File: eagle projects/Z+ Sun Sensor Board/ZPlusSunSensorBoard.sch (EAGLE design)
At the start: 53 parts, among them Q1 BSS138PS,115, Q2 BSS138PS,115, Q7 BSS138PS,115, Q8 BSS138PS,115, U1 ADS7841E_2K5, U2 REF194GSZ-REEL7, U3 TLV9054IDR, U4 LM20BIM7X_NOPB

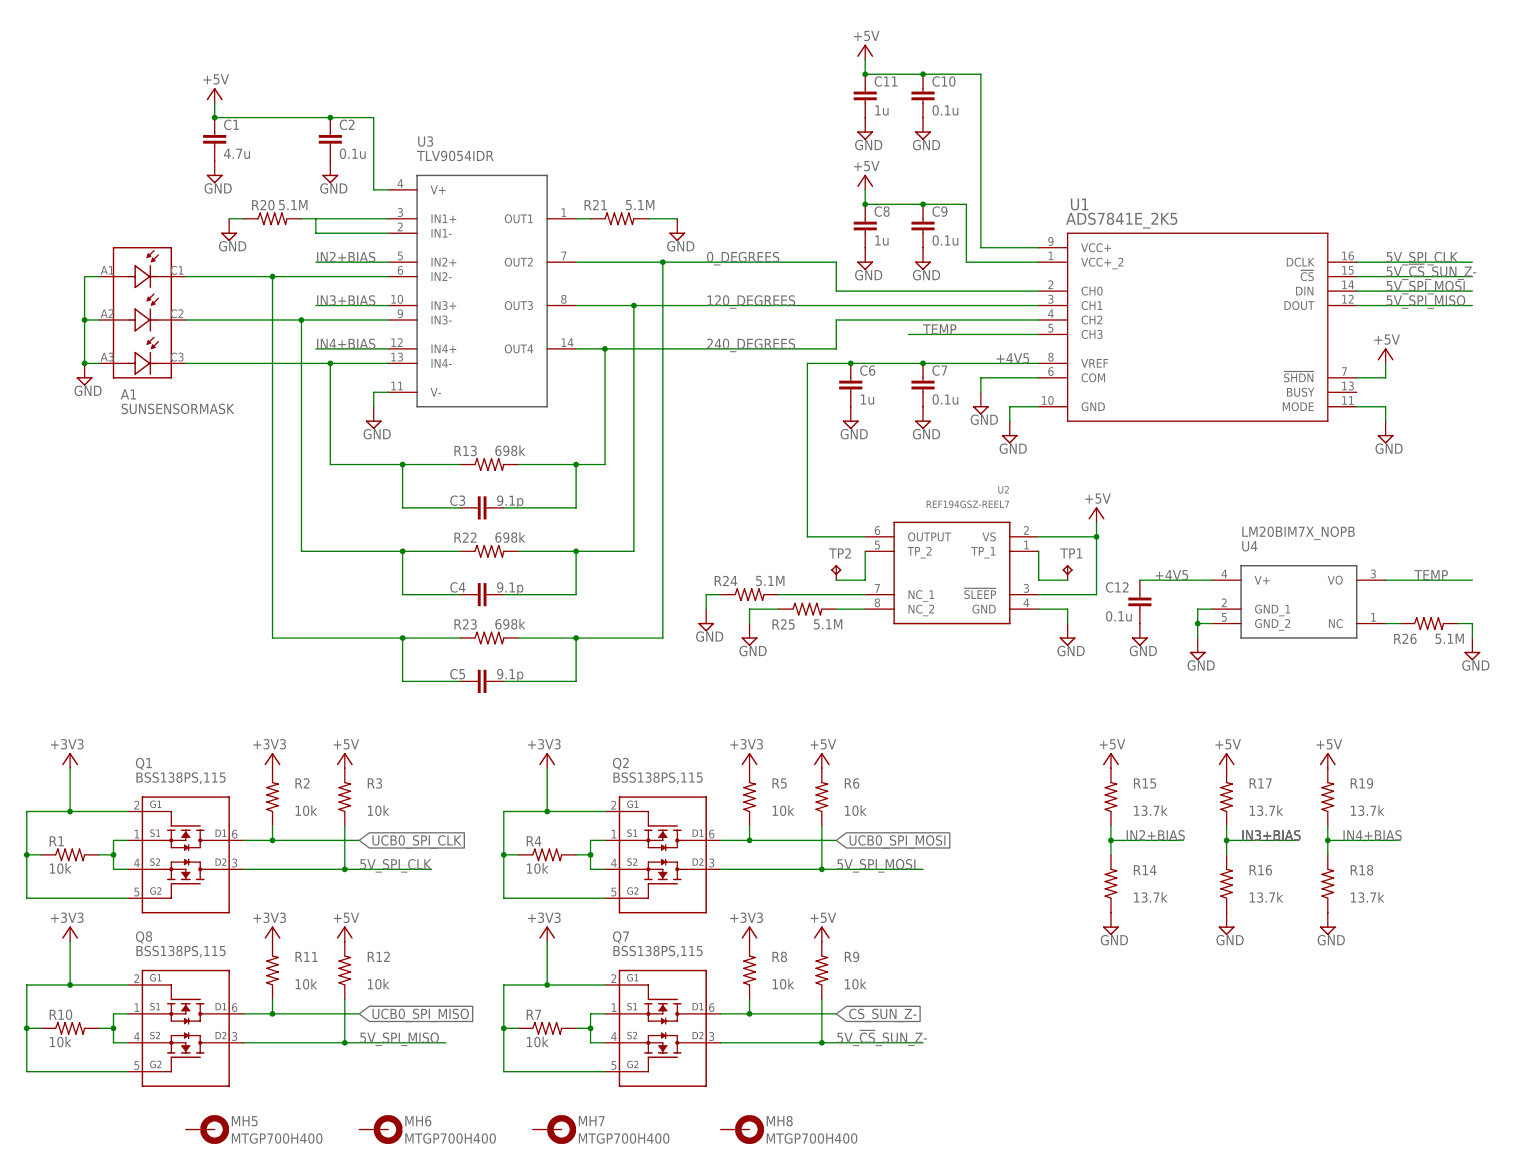
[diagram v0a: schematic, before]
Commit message: Added connector pins
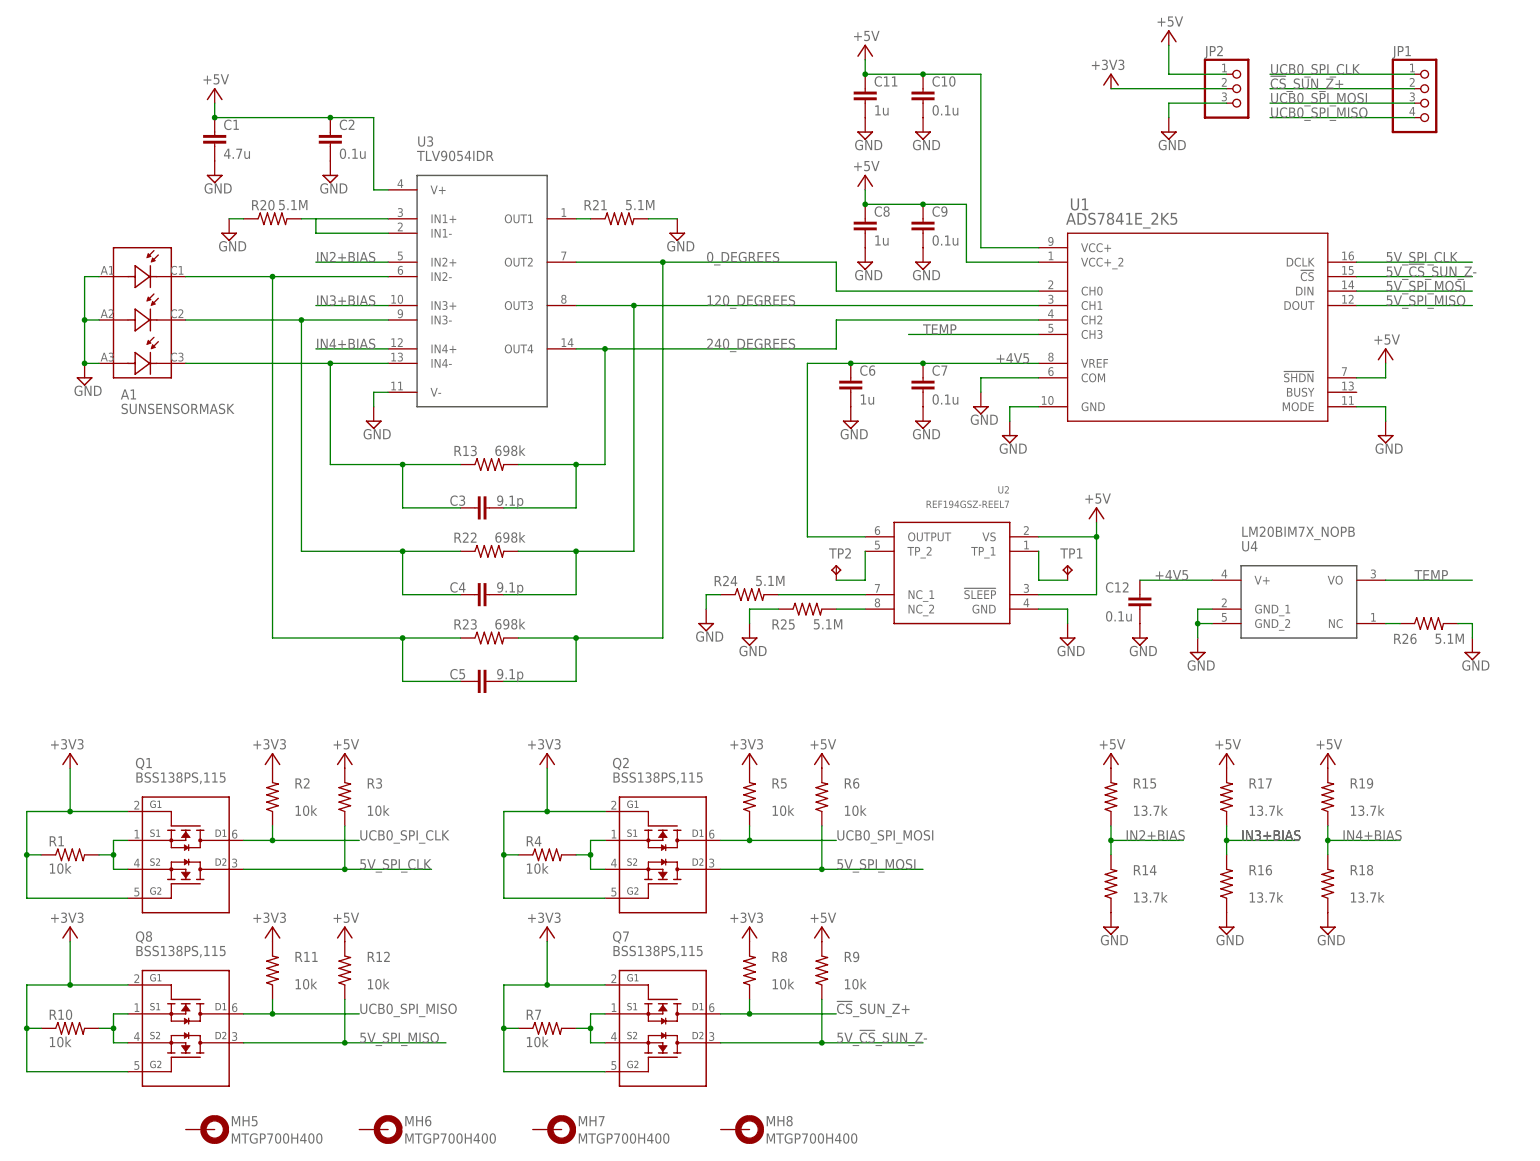
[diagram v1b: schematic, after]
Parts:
- added JP1: (no value), pinhead:PINHD-1X4
- added JP2: (no value), pinhead:PINHD-1X3
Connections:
- removed net !CS!_SUN_Z-: Q7.D1, R8.1
- new net !CS!_SUN_Z+: JP1.2, Q7.D1, R8.1
- net +3V3: now also JP2.2
- net +5V: now also JP2.1
- net GND: now also JP2.3
- net UCB0_SPI_CLK: now also JP1.1
- net UCB0_SPI_MISO: now also JP1.4
- net UCB0_SPI_MOSI: now also JP1.3
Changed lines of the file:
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@@
 <part name="C12" library="rcl" library_urn="urn:adsk.eagle:library:334" deviceset="C-EU" device="C0603" package3d_urn="urn:adsk.eagle:package:23616/2" value="0.1u"/>
 <part name="SUPPLY24" library="supply2" library_urn="urn:adsk.eagle:library:372" deviceset="GND" device=""/>
+<part name="JP1" library="pinhead" library_urn="urn:adsk.eagle:library:325" deviceset="PINHD-1X4" device="" package3d_urn="urn:adsk.eagle:package:22407/2"/>
+<part name="JP2" library="pinhead" library_urn="urn:adsk.eagle:library:325" deviceset="PINHD-1X3" device="" package3d_urn="urn:adsk.eagle:package:22458/2"/>
+<part name="P+4" library="supply1" library_urn="urn:adsk.eagle:library:371" deviceset="+5V" device=""/>
+<part name="+3V9" library="supply1" library_urn="urn:adsk.eagle:library:371" deviceset="+3V3" device=""/>
+<part name="SUPPLY25" library="supply2" library_urn="urn:adsk.eagle:library:372" deviceset="GND" device=""/>
 </parts>
 <sheets>
@@
 <attribute name="VALUE" x="203.835" y="93.345" size="1.778" layer="96"/>
 </instance>
+<instance part="JP1" gate="A" x="256.54" y="190.5" smashed="yes">
+<attribute name="NAME" x="250.19" y="198.755" size="1.778" layer="95"/>
+<attribute name="VALUE" x="250.19" y="182.88" size="1.778" layer="96"/>
+</instance>
+<instance part="JP2" gate="A" x="223.52" y="193.04" smashed="yes">
+<attribute name="NAME" x="217.17" y="198.755" size="1.778" layer="95"/>
+<attribute name="VALUE" x="217.17" y="185.42" size="1.778" layer="96"/>
+</instance>
+<instance part="P+4" gate="1" x="210.82" y="203.2" smashed="yes">
+<attribute name="VALUE" x="213.36" y="205.74" size="1.778" layer="96" rot="R180"/>
+</instance>
+<instance part="+3V9" gate="G$1" x="200.66" y="195.58" smashed="yes">
+<attribute name="VALUE" x="203.2" y="198.12" size="1.778" layer="96" rot="R180"/>
+</instance>
+<instance part="SUPPLY25" gate="GND" x="210.82" y="185.42" smashed="yes">
+<attribute name="VALUE" x="208.915" y="182.245" size="1.778" layer="96"/>
+</instance>
 </instances>
 <busses>
@@
 <wire x1="248.92" y1="142.24" x2="248.92" y2="144.78" width="0.1524" layer="91"/>
 </segment>
+<segment>
+<pinref part="JP2" gate="A" pin="1"/>
+<wire x1="220.98" y1="195.58" x2="210.82" y2="195.58" width="0.1524" layer="91"/>
+<wire x1="210.82" y1="195.58" x2="210.82" y2="200.66" width="0.1524" layer="91"/>
+<pinref part="P+4" gate="1" pin="+5V"/>
+</segment>
 </net>
 <net name="UCB0_SPI_MOSI" class="0">
@@
 <wire x1="137.16" y1="60.96" x2="152.4" y2="60.96" width="0.1524" layer="91"/>
 <junction x="137.16" y="60.96"/>
-<label x="152.4" y="60.96" size="1.778" layer="95" xref="yes"/>
+<label x="152.4" y="60.96" size="1.778" layer="95"/>
+</segment>
+<segment>
+<pinref part="JP1" gate="A" pin="3"/>
+<wire x1="254" y1="190.5" x2="228.6" y2="190.5" width="0.1524" layer="91"/>
+<label x="228.6" y="190.5" size="1.778" layer="95"/>
 </segment>
 </net>
@@
 <wire x1="53.34" y1="60.96" x2="68.58" y2="60.96" width="0.1524" layer="91"/>
 <junction x="53.34" y="60.96"/>
-<label x="68.58" y="60.96" size="1.778" layer="95" xref="yes"/>
+<label x="68.58" y="60.96" size="1.778" layer="95"/>
+</segment>
+<segment>
+<pinref part="JP1" gate="A" pin="1"/>
+<wire x1="254" y1="195.58" x2="228.6" y2="195.58" width="0.1524" layer="91"/>
+<label x="228.6" y="195.58" size="1.778" layer="95"/>
 </segment>
 </net>
@@
 <wire x1="53.34" y1="30.48" x2="68.58" y2="30.48" width="0.1524" layer="91"/>
 <junction x="53.34" y="30.48"/>
-<label x="68.58" y="30.48" size="1.778" layer="95" xref="yes"/>
-</segment>
-</net>
-<net name="!CS!_SUN_Z-" class="0">
+<label x="68.58" y="30.48" size="1.778" layer="95"/>
+</segment>
+<segment>
+<pinref part="JP1" gate="A" pin="4"/>
+<wire x1="254" y1="187.96" x2="228.6" y2="187.96" width="0.1524" layer="91"/>
+<label x="228.6" y="187.96" size="1.778" layer="95"/>
+</segment>
+</net>
+<net name="!CS!_SUN_Z+" class="0">
 <segment>
 <pinref part="Q7" gate="G$1" pin="D1"/>
@@
 <wire x1="137.16" y1="30.48" x2="152.4" y2="30.48" width="0.1524" layer="91"/>
 <junction x="137.16" y="30.48"/>
-<label x="152.4" y="30.48" size="1.778" layer="95" xref="yes"/>
+<label x="152.4" y="30.48" size="1.778" layer="95"/>
+</segment>
+<segment>
+<pinref part="JP1" gate="A" pin="2"/>
+<wire x1="254" y1="193.04" x2="228.6" y2="193.04" width="0.1524" layer="91"/>
+<label x="228.6" y="193.04" size="1.778" layer="95"/>
 </segment>
 </net>
@@
 <wire x1="10.16" y1="35.56" x2="17.78" y2="35.56" width="0.1524" layer="91"/>
 </segment>
+<segment>
+<pinref part="JP2" gate="A" pin="2"/>
+<wire x1="220.98" y1="193.04" x2="200.66" y2="193.04" width="0.1524" layer="91"/>
+<pinref part="+3V9" gate="G$1" pin="+3V3"/>
+</segment>
 </net>
 <net name="N$2" class="0">
@@
 <pinref part="SUPPLY24" gate="GND" pin="GND"/>
 </segment>
-</net>
+<segment>
+<pinref part="JP2" gate="A" pin="3"/>
+<wire x1="220.98" y1="190.5" x2="210.82" y2="190.5" width="0.1524" layer="91"/>
+<wire x1="210.82" y1="190.5" x2="210.82" y2="187.96" width="0.1524" layer="91"/>
+<pinref part="SUPPLY25" gate="GND" pin="GND"/>
+</segment>
+</net>

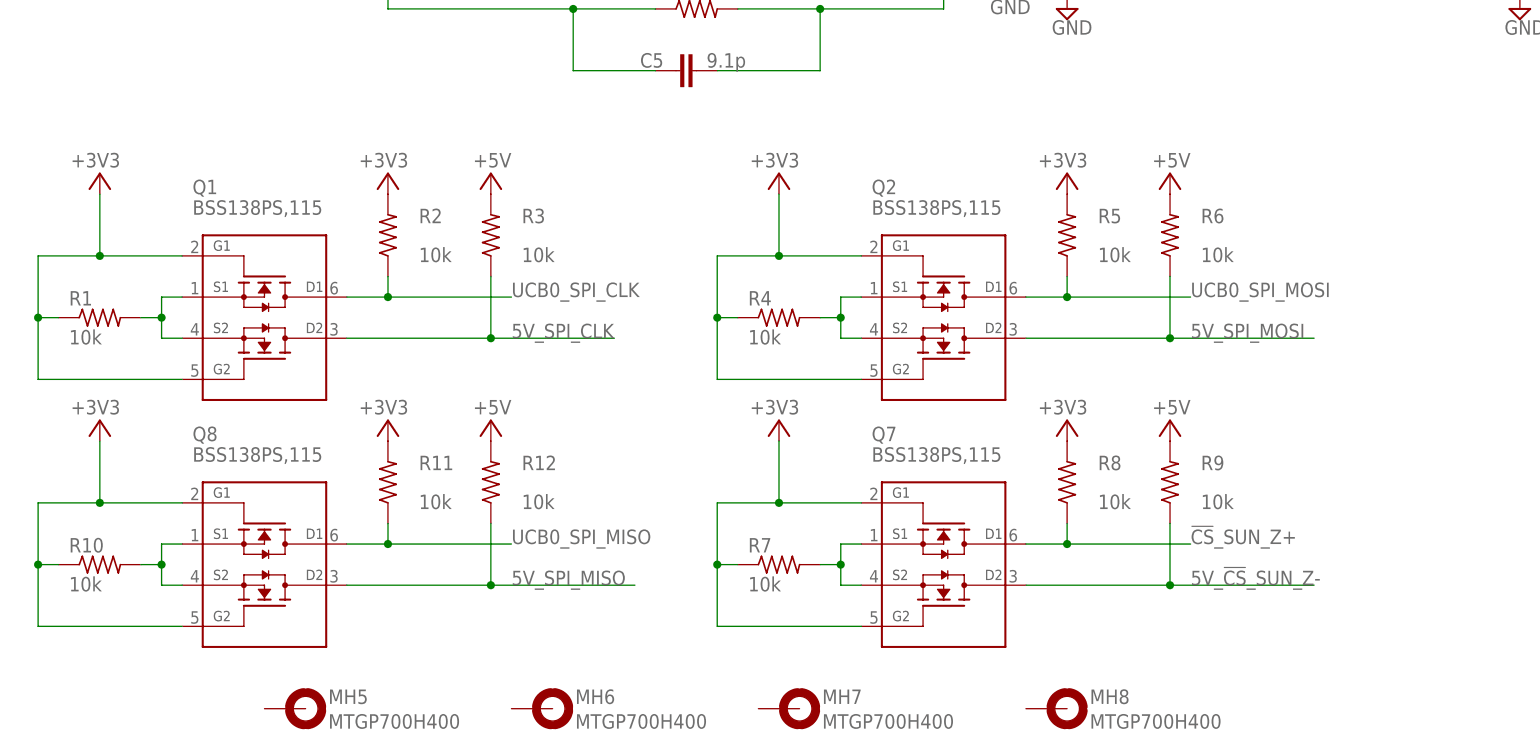
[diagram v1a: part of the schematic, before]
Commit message: Updated logic level shifter mosfet packages and board dimensions
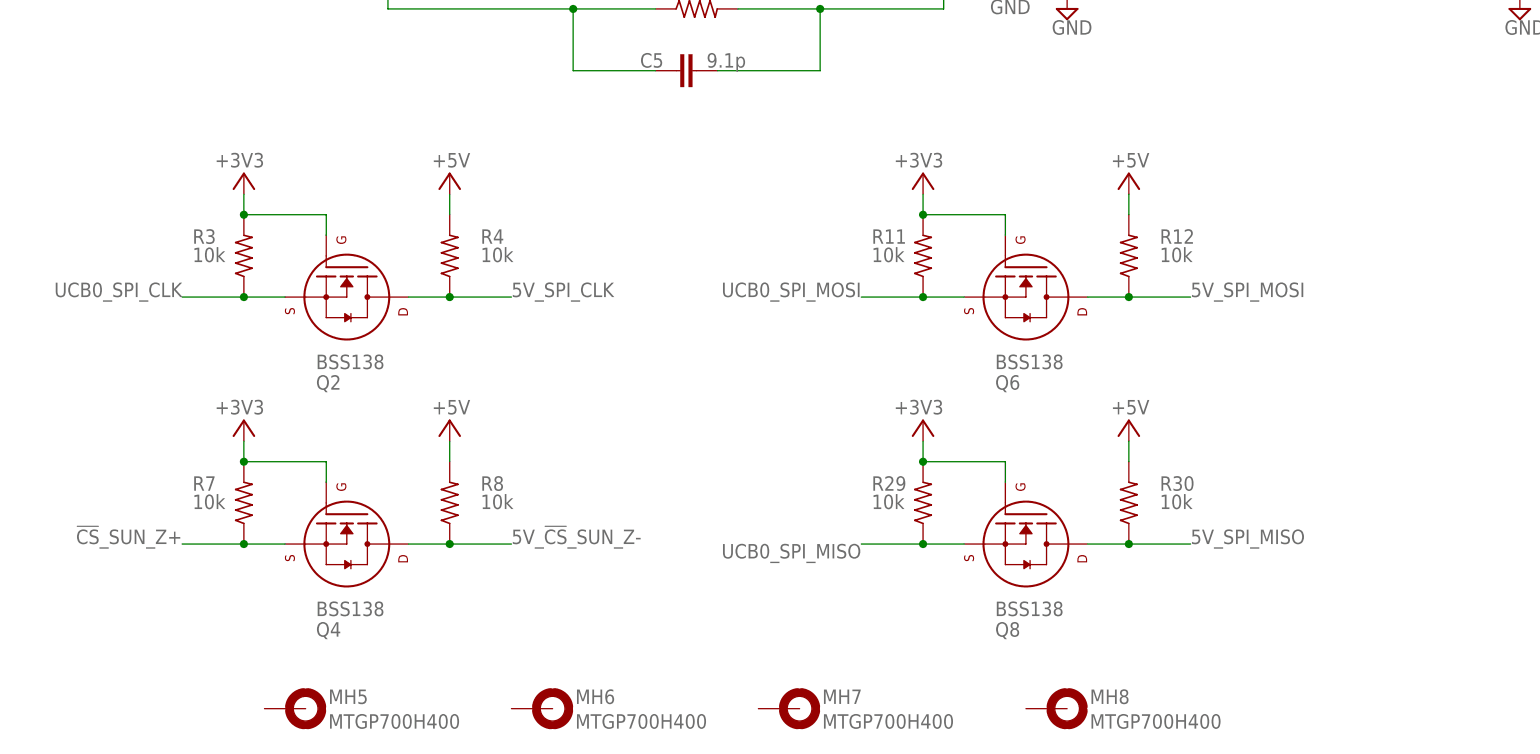
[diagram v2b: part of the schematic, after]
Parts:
- removed Q1, Q7: BSS138PS,115, my_library:BSS138PS,115
- removed R1, R10, R2, R5, R6, R9: 10k, rcl:R-US_R0402
- added Q4, Q6: BSS138, my_library:BSS138
- added R29, R30: 10k, rcl:R-US_R0603
- Q2, Q8: value BSS138PS,115 -> BSS138; device my_library:BSS138PS,115 -> my_library:BSS138
- R11, R12, R3, R4, R7, R8: device rcl:R-US_R0402 -> rcl:R-US_R0603
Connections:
- removed net N$1: Q1.S1, Q1.S2, R1.2
- removed net N$2: Q2.S1, Q2.S2, R4.2
- removed net N$3: Q7.S1, Q7.S2, R7.2
- removed net N$4: Q8.S1, Q8.S2, R10.2
- net !CS!_SUN_Z+: now also Q4.S, R7.1; no longer Q7.D1, R8.1
- net +3V3: now also Q2.G, Q4.G, Q6.G, Q8.G, R29.2, R3.2, R7.2; no longer Q1.G1, Q1.G2, Q2.G1, Q2.G2, Q7.G1, Q7.G2, Q8.G1, Q8.G2, R1.1, R10.1, R2.2, R4.1, R5.2, R7.1, R8.2
- net +5V: now also R30.2, R4.2, R8.2; no longer R3.2, R6.2, R9.2
- net 5V_!CS!_SUN_Z-: now also Q4.D, R8.1; no longer Q7.D2, R9.1
- net 5V_SPI_CLK: now also Q2.D, R4.1; no longer Q1.D2, R3.1
- net 5V_SPI_MISO: now also Q8.D, R30.1; no longer Q8.D2, R12.1
- net 5V_SPI_MOSI: now also Q6.D, R12.1; no longer Q2.D2, R6.1
- net UCB0_SPI_CLK: now also Q2.S, R3.1; no longer Q1.D1, R2.1
- net UCB0_SPI_MISO: now also Q8.S, R29.1; no longer Q8.D1, R11.1
- net UCB0_SPI_MOSI: now also Q6.S, R11.1; no longer Q2.D1, R5.1
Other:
- moved on the sheet: R11, R12, R3, R4, R7, R8
